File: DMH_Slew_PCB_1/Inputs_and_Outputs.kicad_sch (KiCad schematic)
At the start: 7 parts, among them J1 TS_Jack_6.35mm_Sw, J2 TS_Jack_6.35mm_Sw, J200 IDC_02x05, J3 TS_Jack_6.35mm_Sw, J4 TS_Jack_6.35mm_Sw, J50 Conn_01x06, J60 Conn_01x06

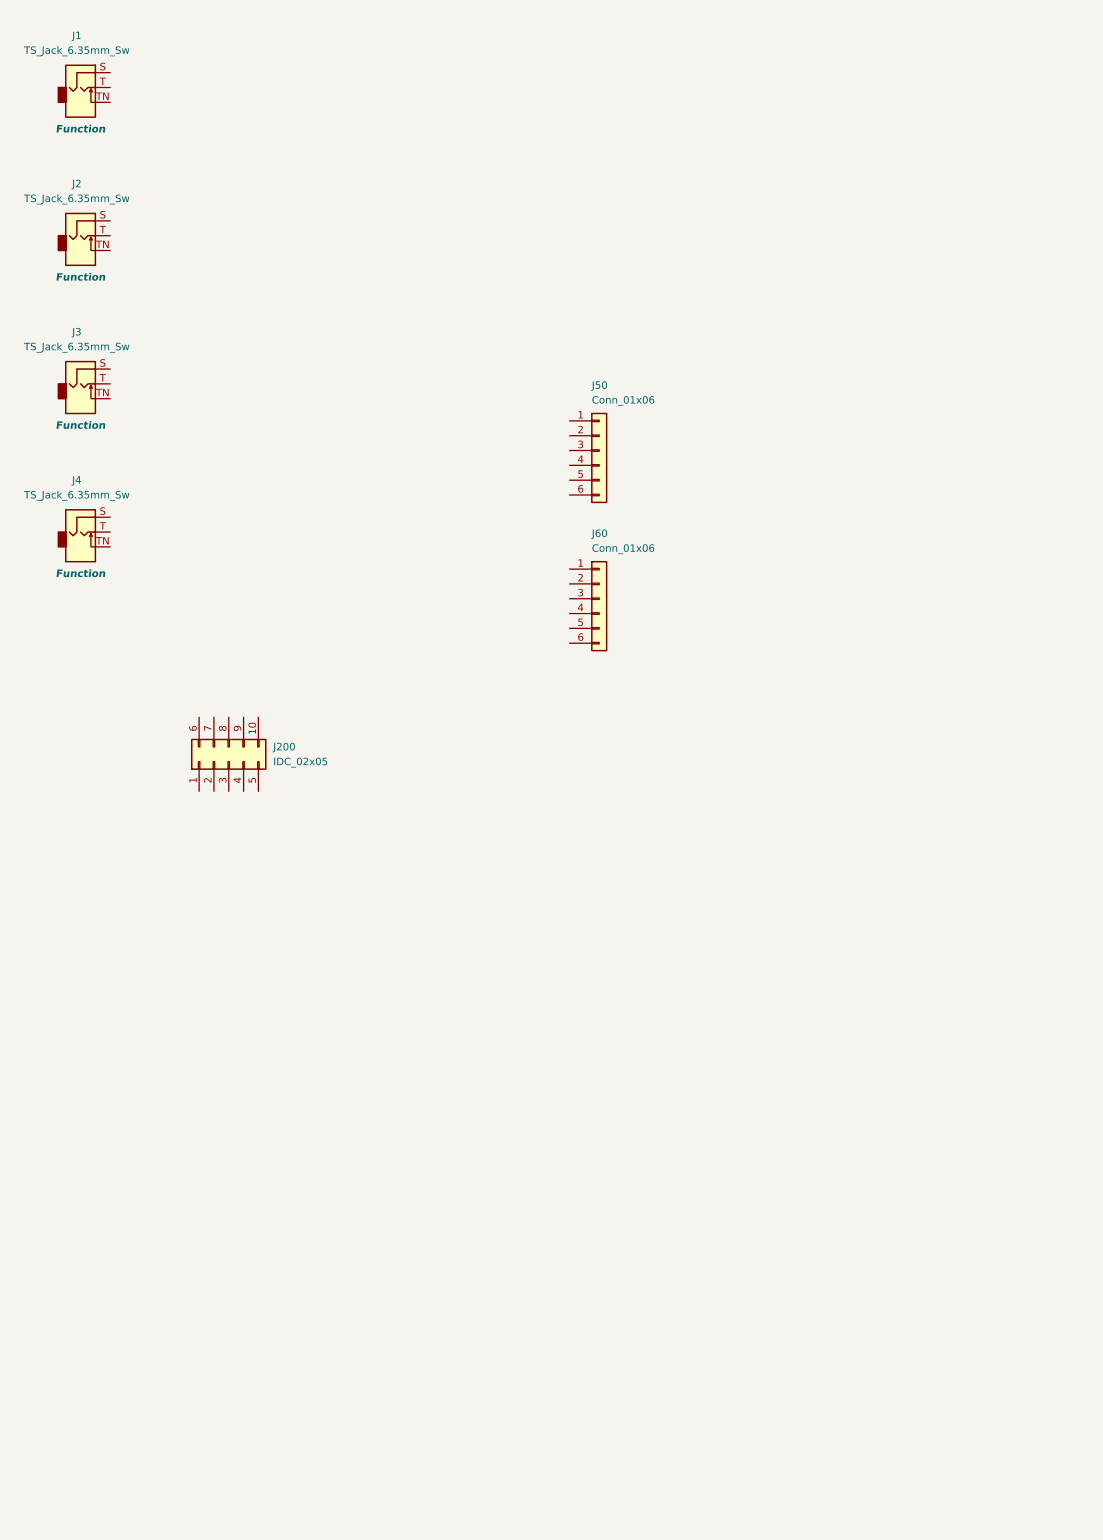
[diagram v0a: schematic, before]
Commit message: Designed IO page
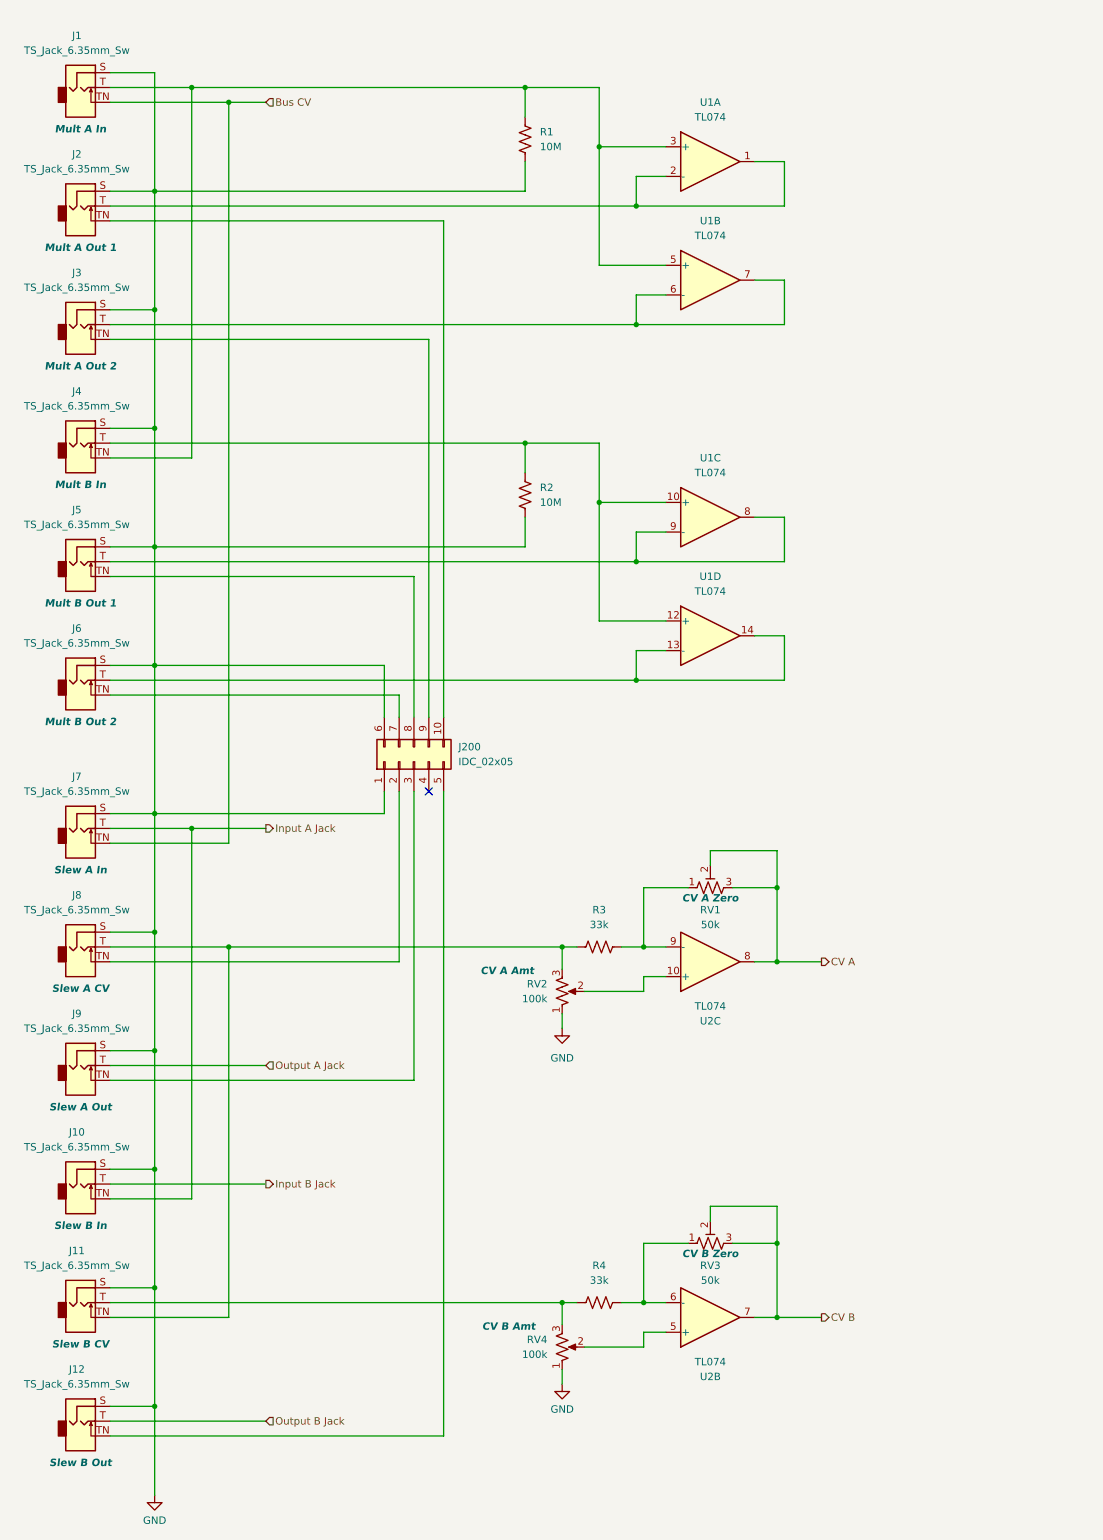
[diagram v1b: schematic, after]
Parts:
- removed J50, J60: Conn_01x06, Connector_PinSocket_2.54mm:PinSocket_1x06_P2.54mm_Vertical, symbol Connector_Generic:Conn_01x06
- added J10, J11, J12, J5, J6, J7, J8, J9: TS_Jack_6.35mm_Sw, SynthStuff:CUI_MJ-63052A, symbol SynthStuff:TS_Jack_6.35mm_Sw
- added R1, R2: 10M, Resistor_THT:R_Axial_DIN0207_L6.3mm_D2.5mm_P7.62mm_Horizontal, symbol Device:R_US
- added R3, R4: 33k, Resistor_THT:R_Axial_DIN0207_L6.3mm_D2.5mm_P7.62mm_Horizontal, symbol Device:R_US
- added RV1, RV3: 50k, Potentiometer_THT:Potentiometer_Bourns_3296X_Horizontal, symbol Device:R_Potentiometer_Trim_US
- added RV2, RV4: 100k, SynthStuff:Potentiometer_TT_P110KH1, symbol Device:R_Potentiometer_US
- added U1, U2: TL074, Package_DIP:DIP-14_W7.62mm_Socket, symbol Amplifier_Operational:TL074
- J1: Function Function -> Mult A In
- J2: Function Function -> Mult A Out 1
- J3: Function Function -> Mult A Out 2
- J4: Function Function -> Mult B In
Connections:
- net GND: now reaches J200.1 (Pin_1)
- net GND: now also J1.S, J2.S, J200.6 (Pin_6), J3.S, J4.S, J10.S, J11.S, J12.S, J5.S, J6.S, J7.S, J8.S, J9.S, R1.1, R2.1, RV2.1, RV4.1
- net at J200.10 (Pin_10): now also J2.TN
- net at J200.2 (Pin_2): now also J8.TN
- net at J200.3 (Pin_3): now also J9.TN
- net at J200.5 (Pin_5): now also J12.TN
- net at J200.7 (Pin_7): now also J6.TN
- net at J200.8 (Pin_8): now also J5.TN
- net at J200.9 (Pin_9): now also J3.TN
- net at J3.T: now also U1.6 (-), U1.7
- net at J4.T: now also R2.2, U1.10 (+), U1.12 (+)
- net at J4.TN: now also J1.T, R1.2, U1.3 (+), U1.5 (+)
- net Bus CV: now reaches J1.TN
- net Bus CV: now also J7.TN
- net at J2.T: now also U1.1, U1.2 (-)
- new net: J11.T, R4.1, RV4.3
- new net: J11.TN, J8.T, R3.1, RV2.3
- new net: RV4.2, U2.5 (+)
- new net: R4.2, RV3.1, U2.6 (-)
- new net: J6.T, U1.13 (-), U1.14
- new net: R3.2, RV1.1, U2.9 (-)
- new net: J5.T, U1.8, U1.9 (-)
- new net: RV2.2, U2.10 (+)
- new net CV A: RV1.2, RV1.3, U2.8
- new net CV B: RV3.2, RV3.3, U2.7
- new net Input A Jack: J10.TN, J7.T
- new net Input B Jack: J10.T
- new net Output A Jack: J9.T
- new net Output B Jack: J12.T
- no-connect marks 0 -> 1
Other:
- moved on the sheet: J2, J200, J3, J4

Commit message: Fixed normalization and started simulation
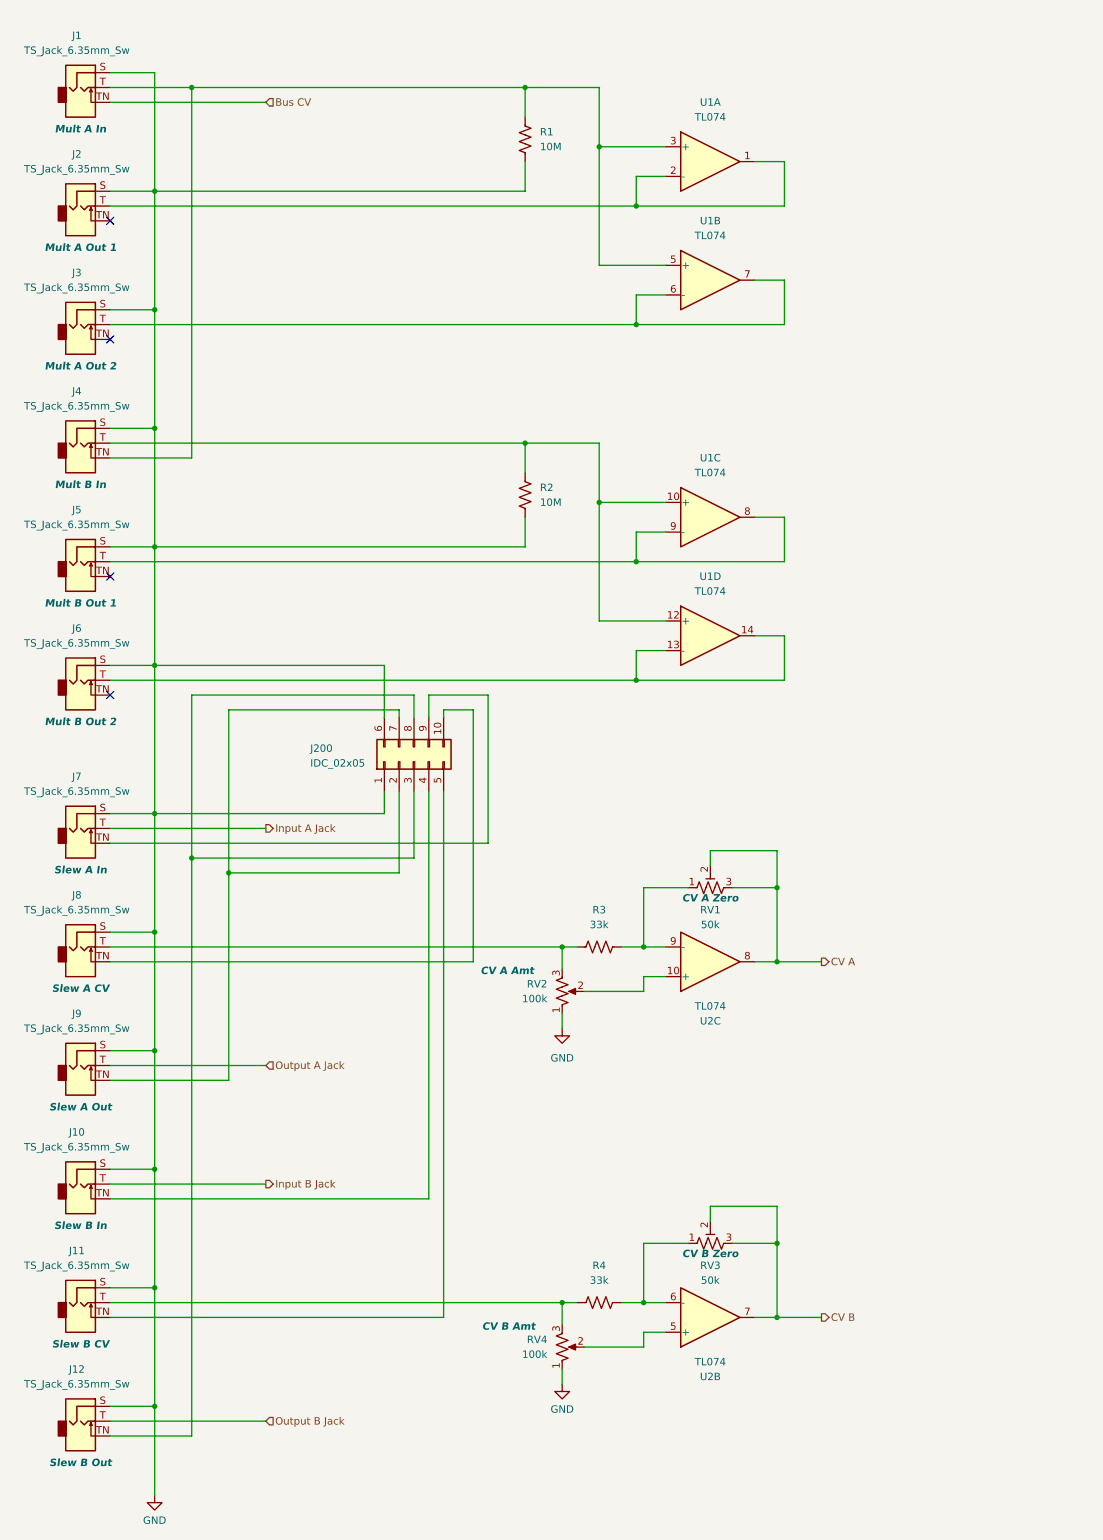
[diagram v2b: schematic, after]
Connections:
- net Bus CV: no longer J7.TN
- net Input A Jack: no longer J10.TN
- net at J8.T, R3.1, RV2.3: no longer J11.TN
- net at J200.5 (Pin_5): now also J11.TN; no longer J12.TN
- net at J200.10 (Pin_10): now also J8.TN; no longer J2.TN
- net at J200.2 (Pin_2): now also J200.7 (Pin_7), J9.TN; no longer J8.TN
- net at J200.3 (Pin_3): now also J12.TN, J200.8 (Pin_8); no longer J9.TN
- net at J200.4 (Pin_4): now also J10.TN
- net at J6.TN: no longer J200.7 (Pin_7)
- net at J5.TN: no longer J200.8 (Pin_8)
- net at J200.9 (Pin_9): now also J7.TN; no longer J3.TN
- no-connect marks 1 -> 4

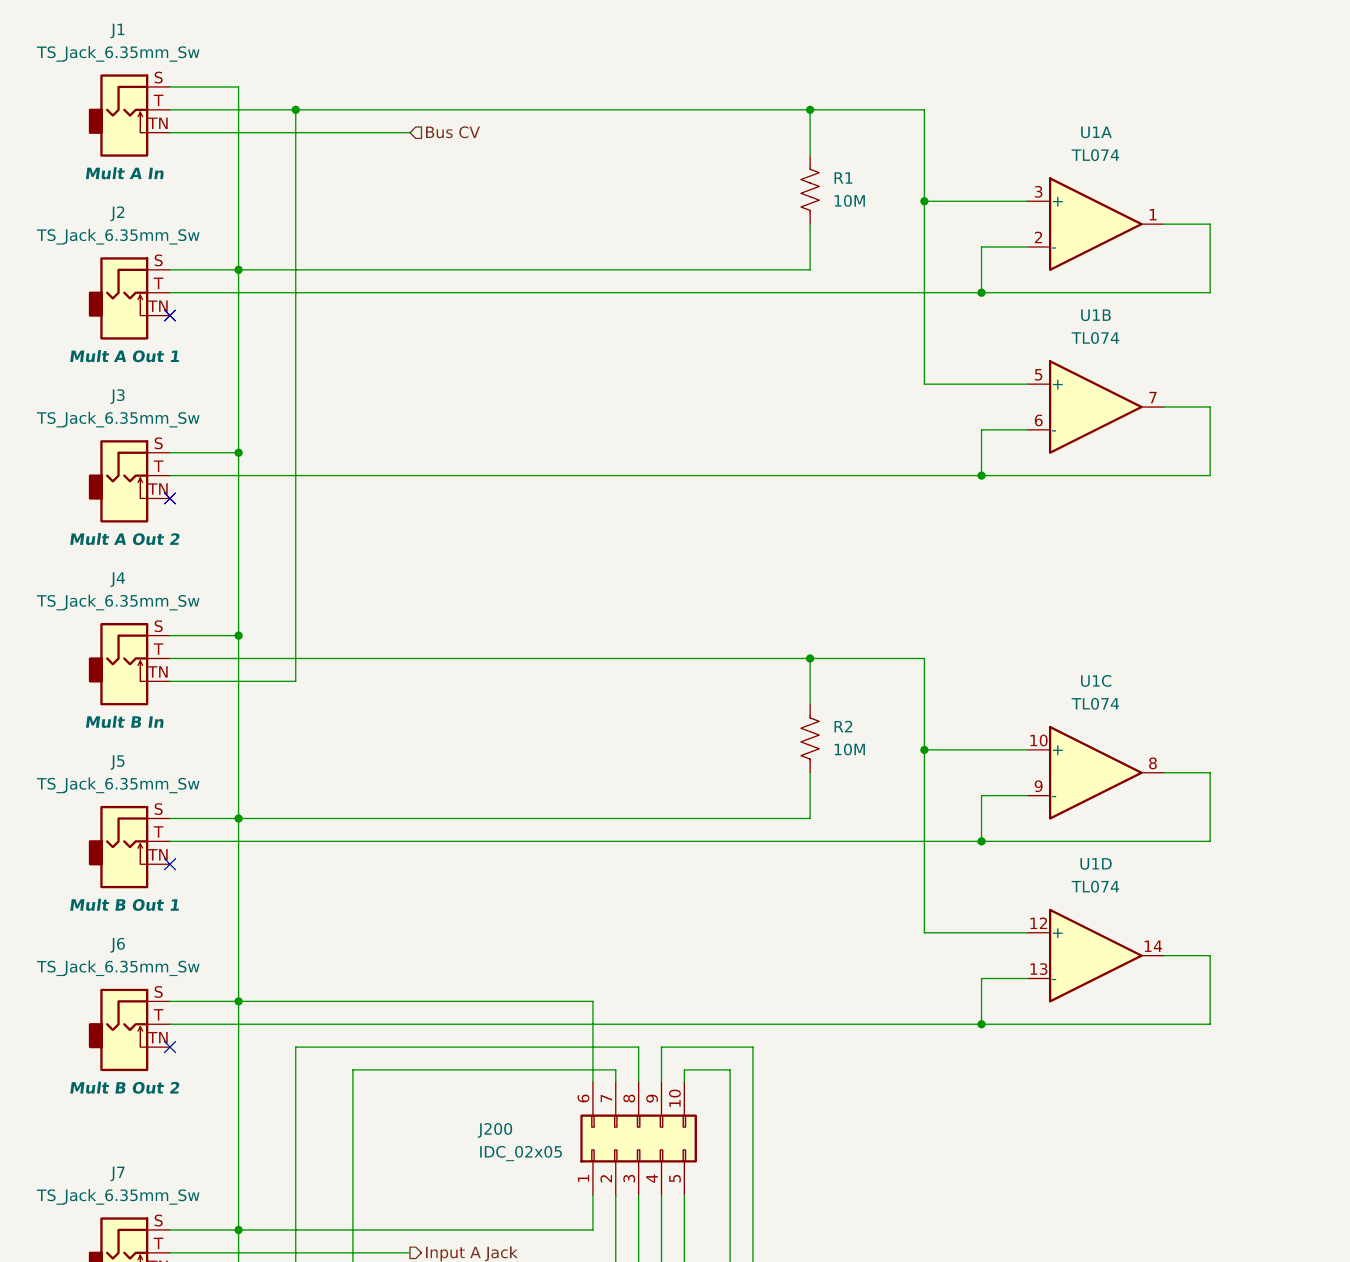
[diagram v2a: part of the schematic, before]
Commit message: Update Inputs_and_Outputs.kicad_sch
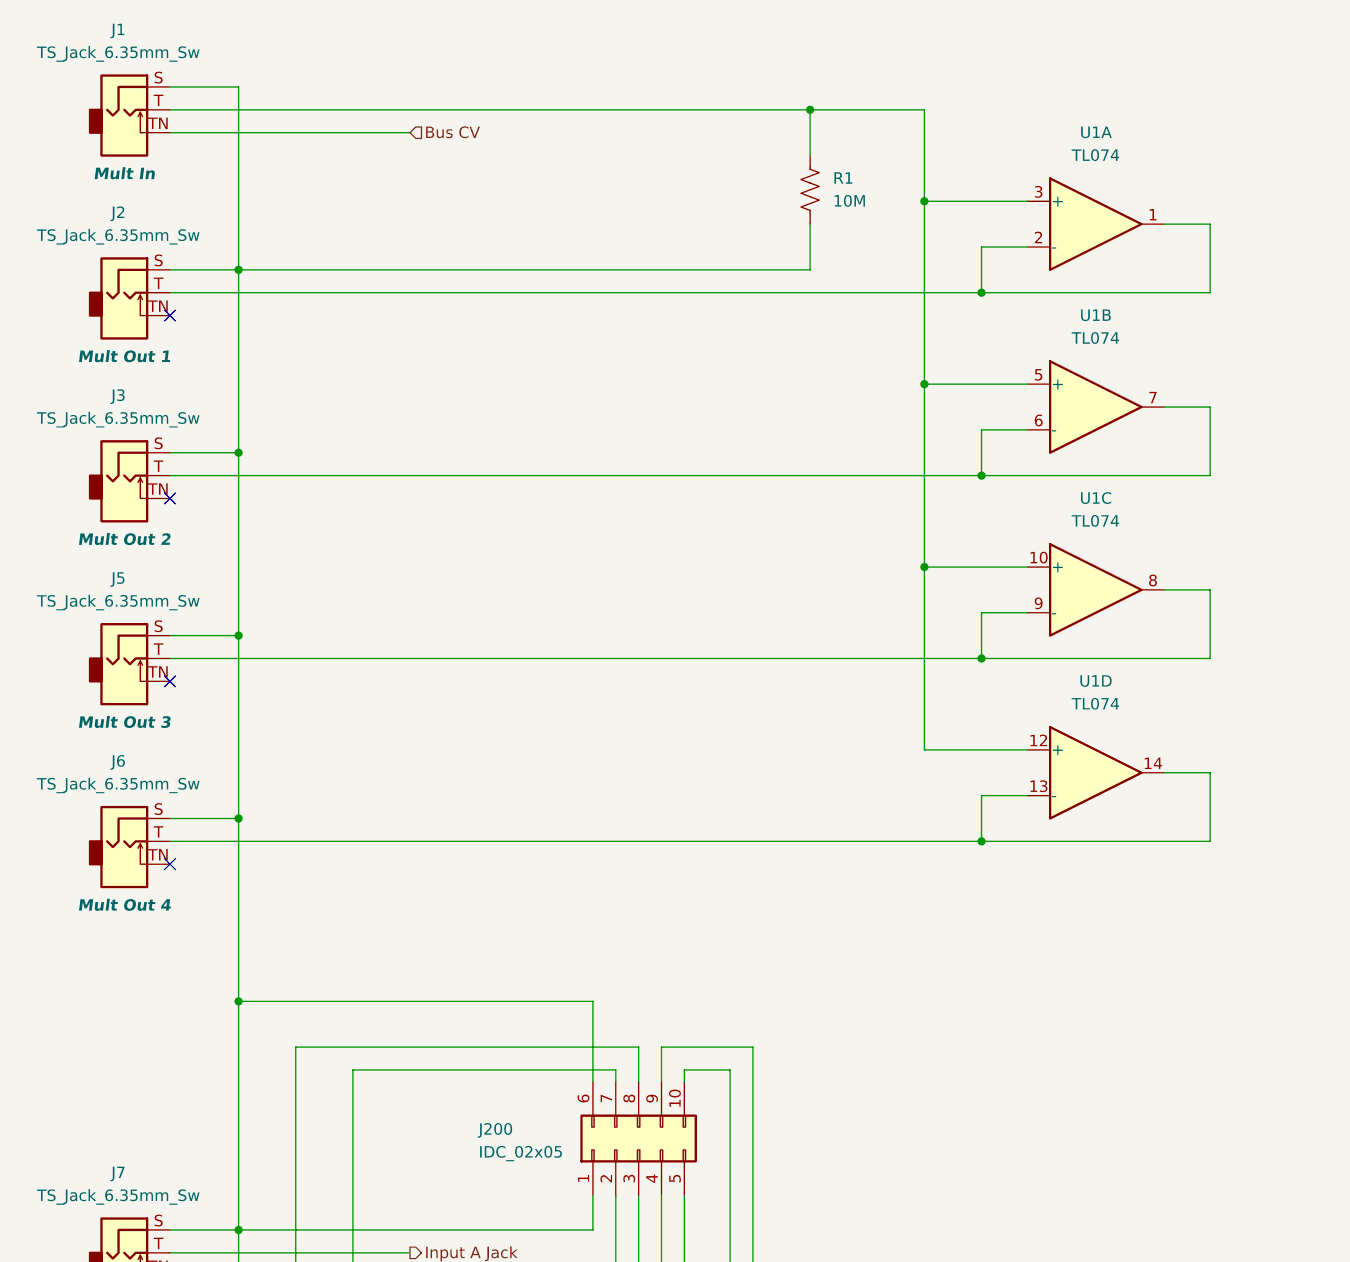
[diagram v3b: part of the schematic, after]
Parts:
- removed J4: TS_Jack_6.35mm_Sw, SynthStuff:CUI_MJ-63052A, symbol SynthStuff:TS_Jack_6.35mm_Sw
- removed R2: 10M, Resistor_THT:R_Axial_DIN0207_L6.3mm_D2.5mm_P7.62mm_Horizontal, symbol Device:R_US
- J1: Function Mult A In -> Mult In
- J2: Function Mult A Out 1 -> Mult Out 1
- J3: Function Mult A Out 2 -> Mult Out 2
- J5: Function Mult B Out 1 -> Mult Out 3
- J6: Function Mult B Out 2 -> Mult Out 4
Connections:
- net at J1.T, R1.2, U1.3 (+)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: now also U1.10 (+), U1.12 (+)
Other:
- moved on the sheet: J5, J6, U1C, U1D
